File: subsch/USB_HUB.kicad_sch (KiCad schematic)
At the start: 7 parts, among them U12 SL2.1S, Y2 12M

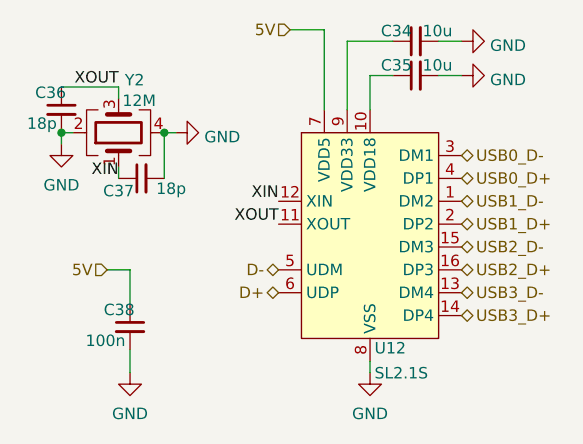
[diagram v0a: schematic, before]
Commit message: Change routings&Add ESD for UART and CAN&Add 5V protection and pull-resistance for GPIO
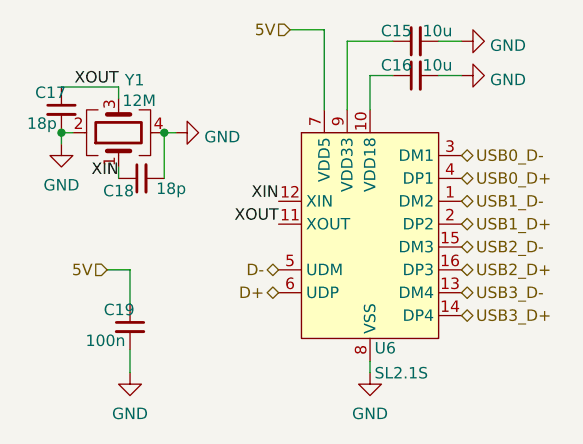
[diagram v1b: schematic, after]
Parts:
- renumbered C34 to C15, C35 to C16, C36 to C17, C37 to C18, C38 to C19, U12 to U6, Y2 to Y1
